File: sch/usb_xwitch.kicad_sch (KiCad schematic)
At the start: 56 parts, among them J4 USB_C_Receptacle, J5 USB3_A, J6 USB_C_Receptacle, J7 USB3_A, J8 Conn_02x05_Odd_Even, J9 C65114, K2 Relay_DPDT_Panasonic_AGQ200A4H, Q1 2N7002P, Q2 2N7002P, Q3 2N7002P, SW1 C2689642

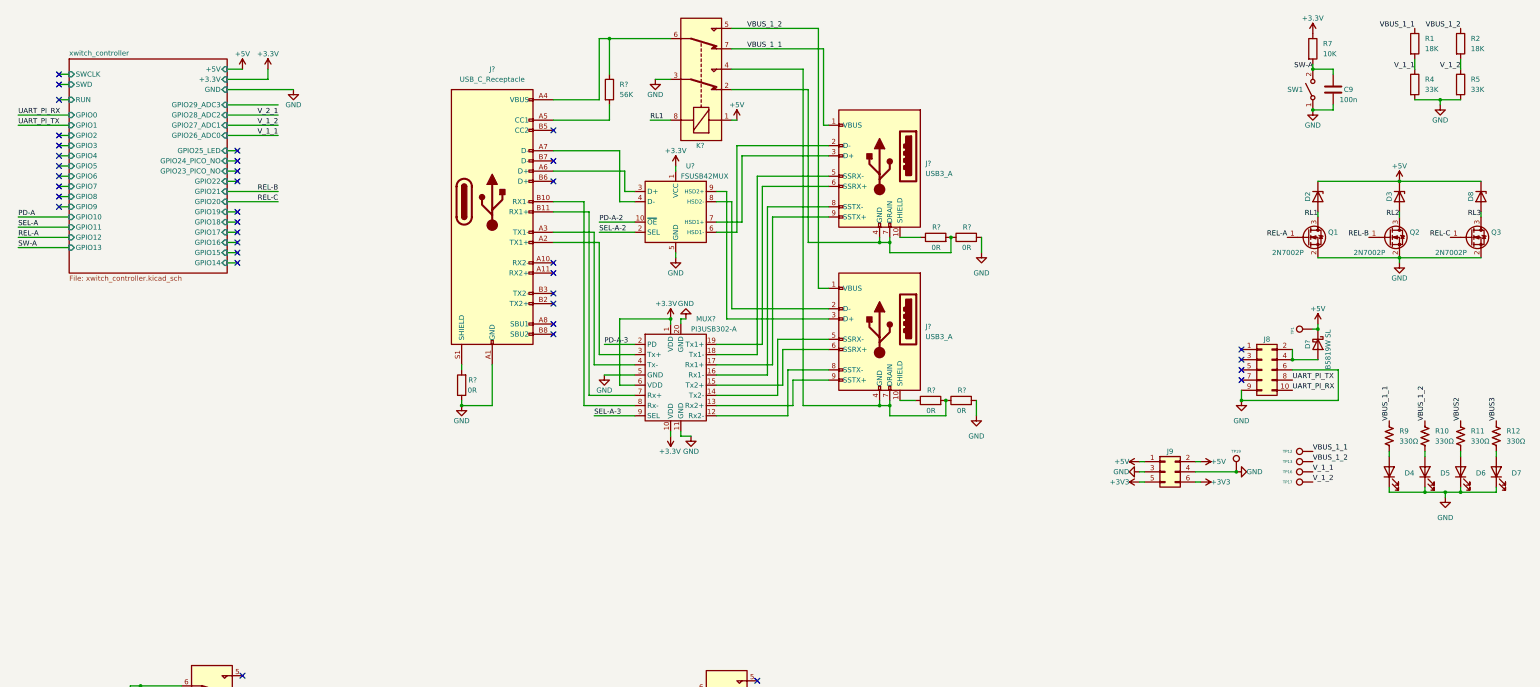
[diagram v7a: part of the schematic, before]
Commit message: added sch boxes
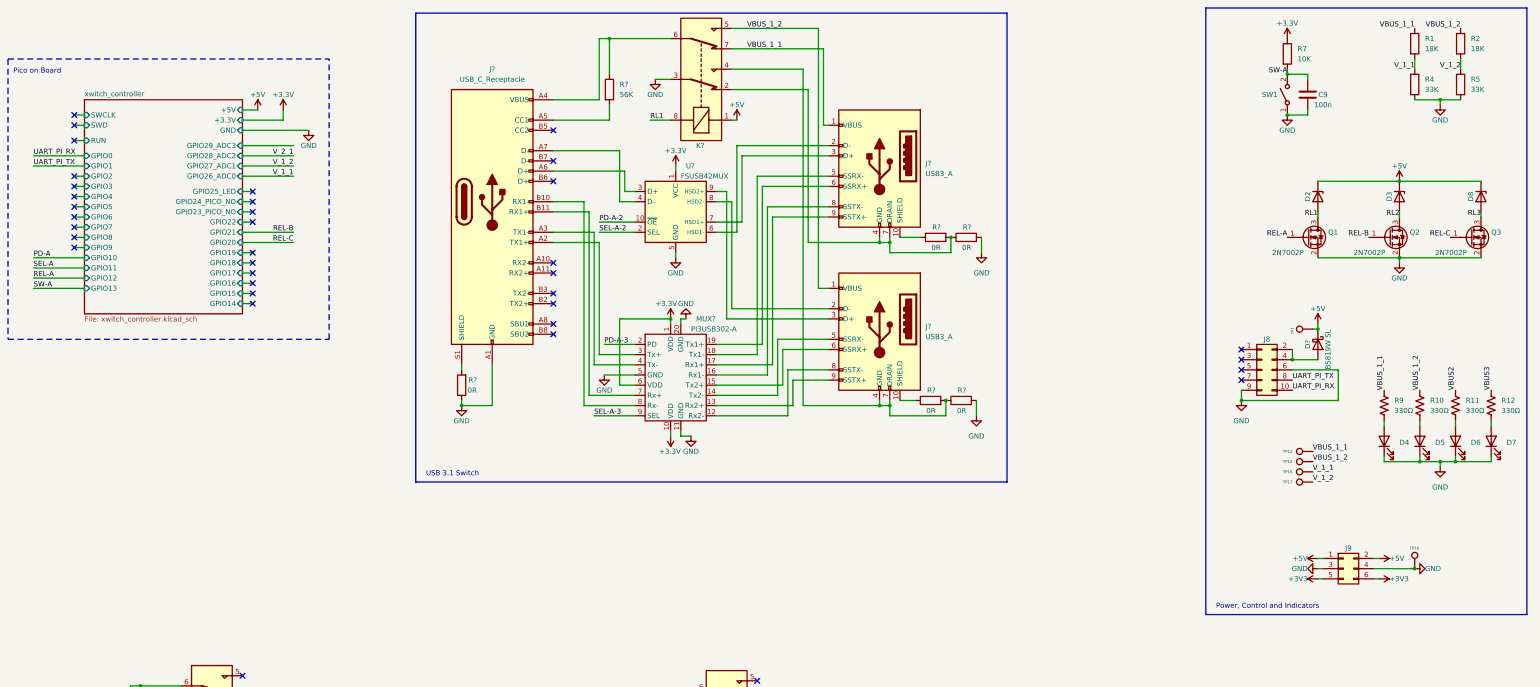
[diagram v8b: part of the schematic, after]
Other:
- note added: "Pico on Board"
- note added: "Power, Control and Indicators"
- note added: "USB 3.1 Switch"
- moved on the sheet: C9, D4, D5, D6, D7, J9, R10, R11, R12, R7, R9, SW1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
